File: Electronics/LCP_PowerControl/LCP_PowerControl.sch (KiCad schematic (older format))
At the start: 0 parts

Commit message: Adding libraries and recent changes
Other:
- note added: "To Do:\n1. 12V Power Regulator\n2. Fix connectors for battery (Use Molex)"
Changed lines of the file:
@@
 $Descr A4 11693 8268
 encoding utf-8
-Sheet 1 8
+Sheet 1 11
 Title "Low Cost Profiler - Power Control Board"
 Date ""
@@
 $EndDescr
 $Sheet
-S 850  1250 1350 1150
+S 850  850  1350 1150
 U 5EE2A57D
 F0 "Battery Input" 50
 F1 "BatteryInput.sch" 50
-F2 "BATT_V+" O R 2200 1550 50
-F3 "BATT_V-" I R 2200 2050 50
-$EndSheet
-$Sheet
-S 2600 1250 1300 1150
+F2 "BATT_V+" O R 2200 1150 50
+F3 "BATT_V-" I R 2200 1650 50
+$EndSheet
+$Sheet
+S 2600 850  1300 1150
 U 5EE2A7AF
 F0 "Power Monitoring" 50
 F1 "PowerMonitoring.sch" 50
-F2 "BM_SDA" B R 3900 1650 50
-F3 "BM_SCL" I R 3900 1800 50
-F4 "BM_IRQ" O R 3900 1950 50
-F5 "BATT_V-" O L 2600 2050 50
-F6 "BATT_V+" I L 2600 1550 50
-$EndSheet
-$Sheet
-S 850  5250 1350 1150
+F2 "BM_SDA" B R 3900 1250 50
+F3 "BM_SCL" I R 3900 1400 50
+F4 "BM_IRQ" O R 3900 1550 50
+F5 "BATT_V-" O L 2600 1650 50
+F6 "BATT_V+" I L 2600 1150 50
+$EndSheet
+$Sheet
+S 850  5350 1350 1150
 U 5EE2A864
 F0 "Console" 50
 F1 "Console.sch" 50
-F2 "CONSOLE_RX" I R 2200 5850 50
-F3 "CONSOLE_TX" O R 2200 6000 50
-F4 "CONSOLE_PWR" O R 2200 5700 50
-$EndSheet
-$Sheet
-S 850  3900 1350 1150
+F2 "CONSOLE_RX" I R 2200 5950 50
+F3 "CONSOLE_TX" O R 2200 6100 50
+F4 "CONSOLE_PWR" O R 2200 5800 50
+$EndSheet
+$Sheet
+S 850  3500 1350 1150
 U 5EE2AA1B
 F0 "Control Board Connection" 50
 F1 "Control.sch" 50
-F2 "CONTROL_SDA" B R 2200 4400 50
-F3 "CONTROL_EN" O R 2200 4250 50
-F4 "CONTROL_SCL" O R 2200 4550 50
-$EndSheet
-$Sheet
-S 8100 2950 1300 1150
+F2 "CONTROL_SDA" B R 2200 4000 50
+F3 "CONTROL_EN" O R 2200 3850 50
+F4 "CONTROL_SCL" O R 2200 4150 50
+$EndSheet
+$Sheet
+S 8100 2550 1300 1150
 U 5EE2AB43
-F0 "Piston Control" 50
+F0 "Piston Driver" 50
 F1 "PistonControl.sch" 50
-F2 "MD_EN" I L 8100 3300 50
-F3 "MD_PH" I L 8100 3400 50
-F4 "~MD_FAULT" O L 8100 3500 50
-F5 "MD_IPROPI" U L 8100 3600 50
-F6 "~MD_SLEEP" I L 8100 3800 50
-F7 "MD_PMODE" I L 8100 3700 50
-F8 "MD_POWER_EN" I L 8100 3200 50
-$EndSheet
-Wire Wire Line
-	2600 2050 2200 2050
-Wire Wire Line
-	2200 1550 2600 1550
-Wire Wire Line
-	4300 1950 3900 1950
-Wire Wire Line
-	3900 1800 4300 1800
-Wire Wire Line
-	4300 1650 3900 1650
-Wire Wire Line
-	2200 4250 4300 4250
-Wire Wire Line
-	4300 4400 2200 4400
-Wire Wire Line
-	2200 4550 4300 4550
-Wire Wire Line
-	4300 5850 2200 5850
-Wire Wire Line
-	2200 6000 4300 6000
-Wire Wire Line
-	8100 3300 7000 3300
+F2 "MD_EN" I L 8100 2900 50
+F3 "MD_PH" I L 8100 3000 50
+F4 "~MD_FAULT" O L 8100 3100 50
+F5 "MD_IPROPI" U L 8100 3200 50
+F6 "~MD_SLEEP" I L 8100 3400 50
+F7 "MD_PMODE" I L 8100 3300 50
+F8 "ACTUATOR_POWER+" O R 9400 3450 50
+F9 "ACTUATOR_POWER-" O R 9400 3550 50
+$EndSheet
+Wire Wire Line
+	2600 1650 2200 1650
+Wire Wire Line
+	2200 1150 2600 1150
+Wire Wire Line
+	4300 1550 3900 1550
+Wire Wire Line
+	3900 1400 4300 1400
+Wire Wire Line
+	4300 1250 3900 1250
+Wire Wire Line
+	2200 3850 4300 3850
+Wire Wire Line
+	4300 4000 2200 4000
+Wire Wire Line
+	2200 4150 4300 4150
+Wire Wire Line
+	4300 5950 2200 5950
+Wire Wire Line
+	2200 6100 4300 6100
+Wire Wire Line
+	8100 2900 7000 2900
+Wire Wire Line
+	7000 3000 8100 3000
+Wire Wire Line
+	7000 3100 8100 3100
+Wire Wire Line
+	8100 3200 7000 3200
+Wire Wire Line
+	7000 3300 8100 3300
 Wire Wire Line
 	7000 3400 8100 3400
-Wire Wire Line
-	7000 3500 8100 3500
-Wire Wire Line
-	8100 3600 7000 3600
-Wire Wire Line
-	7000 3700 8100 3700
-Wire Wire Line
-	7000 3800 8100 3800
-$Sheet
-S 2600 2700 1300 1150
+$Sheet
+S 2600 2300 1300 1150
 U 5EE4388C
 F0 "Power Regulators" 50
 F1 "PowerRegulators.sch" 50
-F2 "POWER_EN" I R 3900 3050 50
-$EndSheet
-Wire Wire Line
-	7000 3200 8100 3200
-Wire Wire Line
-	3900 3050 4300 3050
-$Sheet
-S 4300 1250 2700 5150
+F2 "POWER_EN" I R 3900 2650 50
+$EndSheet
+Wire Wire Line
+	3900 2650 4300 2650
+$Sheet
+S 4300 850  2700 5650
 U 5EE2A5A7
 F0 "Microcontroller" 50
 F1 "Microcontroller.sch" 50
-F2 "BM_SDA" B L 4300 1650 50
-F3 "BM_SCL" O L 4300 1800 50
-F4 "BM_IRQ" I L 4300 1950 50
-F5 "CONTROL_EN" I L 4300 4250 50
-F6 "CONTROL_SDA" B L 4300 4400 50
-F7 "CONTROL_SCL" I L 4300 4550 50
-F8 "CONSOLE_TX" I L 4300 6000 50
-F9 "CONSOLE_RX" O L 4300 5850 50
-F10 "MD_EN" O R 7000 3300 50
-F11 "MD_PH" O R 7000 3400 50
-F12 "~MD_FAULT" I R 7000 3500 50
-F13 "MD_IPROPI" U R 7000 3600 50
-F14 "MD_PMODE" O R 7000 3700 50
-F15 "~MD_SLEEP" O R 7000 3800 50
-F16 "12V_ENABLE" O L 4300 3050 50
-F17 "MD_POWER_EN" O R 7000 3200 50
-$EndSheet
+F2 "BM_SDA" B L 4300 1250 50
+F3 "BM_SCL" O L 4300 1400 50
+F4 "BM_IRQ" I L 4300 1550 50
+F5 "CONTROL_EN" I L 4300 3850 50
+F6 "CONTROL_SDA" B L 4300 4000 50
+F7 "CONTROL_SCL" I L 4300 4150 50
+F8 "CONSOLE_TX" I L 4300 6100 50
+F9 "CONSOLE_RX" O L 4300 5950 50
+F10 "MD_EN" O R 7000 2900 50
+F11 "MD_PH" O R 7000 3000 50
+F12 "~MD_FAULT" I R 7000 3100 50
+F13 "MD_IPROPI" U R 7000 3200 50
+F14 "MD_PMODE" O R 7000 3300 50
+F15 "~MD_SLEEP" O R 7000 3400 50
+F16 "12V_ENABLE" O L 4300 2650 50
+F17 "DEBUG_TX" O L 4300 4950 50
+F18 "DEBUG_RX" I L 4300 5050 50
+F19 "DEBUG_LED_1" O L 4300 5150 50
+F20 "DEBUG_LED_2" O L 4300 5250 50
+F21 "ENCODER_CH_A" I R 7000 4550 50
+F22 "ENCODER_CH_B" I R 7000 4650 50
+$EndSheet
+Text Notes 7900 1400 0    100  ~ 0
+To Do:\n1. 12V Power Regulator\n2. Fix connectors for battery (Use Molex)
+$Sheet
+S 8100 4050 1300 1150
+U 5EE7B8CC
+F0 "Position Sensing" 50
+F1 "PositionSensing.sch" 50
+F2 "HALL_EFFECT_V+" O R 9400 4150 50
+F3 "HALL_EFFECT_CH_A" I R 9400 4250 50
+F4 "HALL_EFFECT_V-" O R 9400 4450 50
+F5 "HALL_EFFECT_CH_B" I R 9400 4350 50
+F6 "ENCODER_CH_A" I L 8100 4550 50
+F7 "ENCODER_CH_B" I L 8100 4650 50
+$EndSheet
+$Sheet
+S 9850 3300 1300 1150
+U 5EE7B956
+F0 "Actuator Connector" 50
+F1 "ActuatorConnector.sch" 50
+F2 "ACTUATOR_POWER+" I L 9850 3450 50
+F3 "ACTUATOR_POWER-" I L 9850 3550 50
+F4 "HALL_EFFECT_V+" I L 9850 4000 50
+F5 "HALL_EFFECT_CH_A" O L 9850 4100 50
+F6 "HALL_EFFECT_CHB" O L 9850 4200 50
+F7 "HALL_EFFECT_V-" I L 9850 4300 50
+$EndSheet
+Wire Wire Line
+	9400 3450 9850 3450
+Wire Wire Line
+	9850 3550 9400 3550
+Wire Wire Line
+	9400 4150 9550 4150
+Wire Wire Line
+	9550 4150 9550 4000
+Wire Wire Line
+	9550 4000 9850 4000
+Wire Wire Line
+	9400 4250 9600 4250
+Wire Wire Line
+	9600 4250 9600 4100
+Wire Wire Line
+	9600 4100 9850 4100
+Wire Wire Line
+	9400 4350 9650 4350
+Wire Wire Line
+	9650 4350 9650 4200
+Wire Wire Line
+	9650 4200 9850 4200
+Wire Wire Line
+	9400 4450 9700 4450
+Wire Wire Line
+	9700 4450 9700 4300
+Wire Wire Line
+	9700 4300 9850 4300
+Wire Wire Line
+	7000 4550 8100 4550
+Wire Wire Line
+	8100 4650 7000 4650
+$Sheet
+S 2600 4500 1300 1150
+U 5EF8E8EB
+F0 "Debug" 50
+F1 "Debug.sch" 50
+F2 "DEBUG_TX" I R 3900 4950 50
+F3 "DEBUG_RX" O R 3900 5050 50
+F4 "DEBUG_LED_1" I R 3900 5150 50
+F5 "DEBUG_LED_2" I R 3900 5250 50
+$EndSheet
+Wire Wire Line
+	3900 5250 4300 5250
+Wire Wire Line
+	4300 5150 3900 5150
+Wire Wire Line
+	3900 5050 4300 5050
+Wire Wire Line
+	4300 4950 3900 4950
 $EndSCHEMATC

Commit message: Aiming for rev 0.1 complete
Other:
- note removed: "To Do:\n1. 12V Power Regulator\n2. Fix connectors for battery (Use Molex)"
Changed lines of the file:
@@
 Sheet 1 11
 Title "Low Cost Profiler - Power Control Board"
-Date ""
-Rev ""
+Date "2020-06-17"
+Rev "R0.1"
 Comp "NOAA Pacific Marine Environmental Lab"
 Comment1 "Design by: Matt Casari"
@@
 F0 "Power Regulators" 50
 F1 "PowerRegulators.sch" 50
-F2 "POWER_EN" I R 3900 2650 50
+F2 "12V_ENABLE" I R 3900 2650 50
 $EndSheet
 Wire Wire Line
@@
 F22 "ENCODER_CH_B" I R 7000 4650 50
 $EndSheet
-Text Notes 7900 1400 0    100  ~ 0
-To Do:\n1. 12V Power Regulator\n2. Fix connectors for battery (Use Molex)
 $Sheet
 S 8100 4050 1300 1150

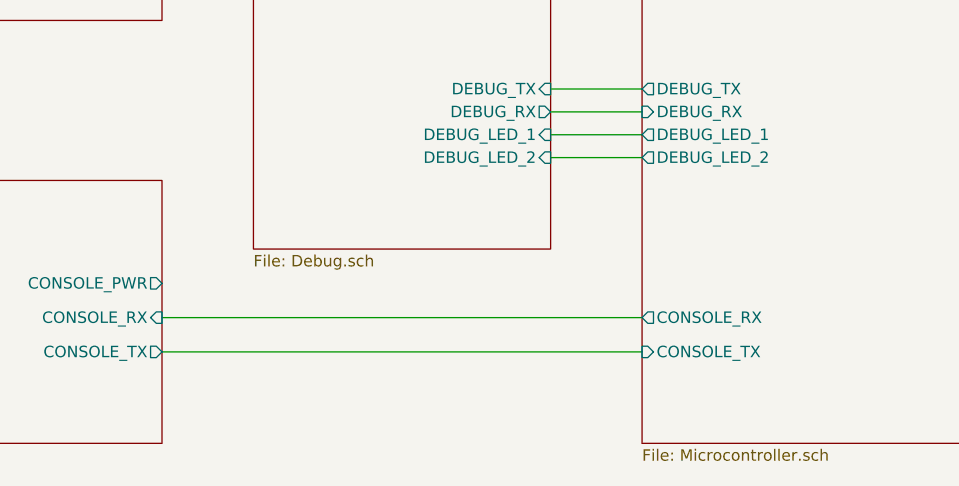
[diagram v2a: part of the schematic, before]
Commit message: Rev1
Removed test points. Cleaned up unnecessary traces. Fixed electrical issues #1-#7
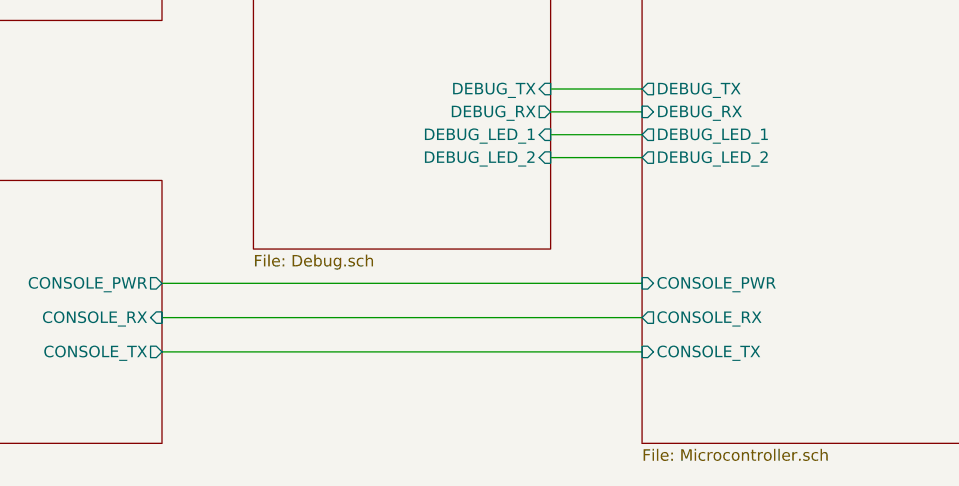
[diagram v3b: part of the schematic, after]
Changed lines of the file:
@@
 F21 "ENCODER_CH_A" I R 7000 4550 50
 F22 "ENCODER_CH_B" I R 7000 4650 50
+F23 "CONSOLE_PWR" I L 4300 5800 50
 $EndSheet
 $Sheet
@@
 Wire Wire Line
 	4300 4950 3900 4950
+Wire Wire Line
+	4300 5800 2200 5800
 $EndSCHEMATC
